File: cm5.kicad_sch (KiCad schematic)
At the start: 22 parts

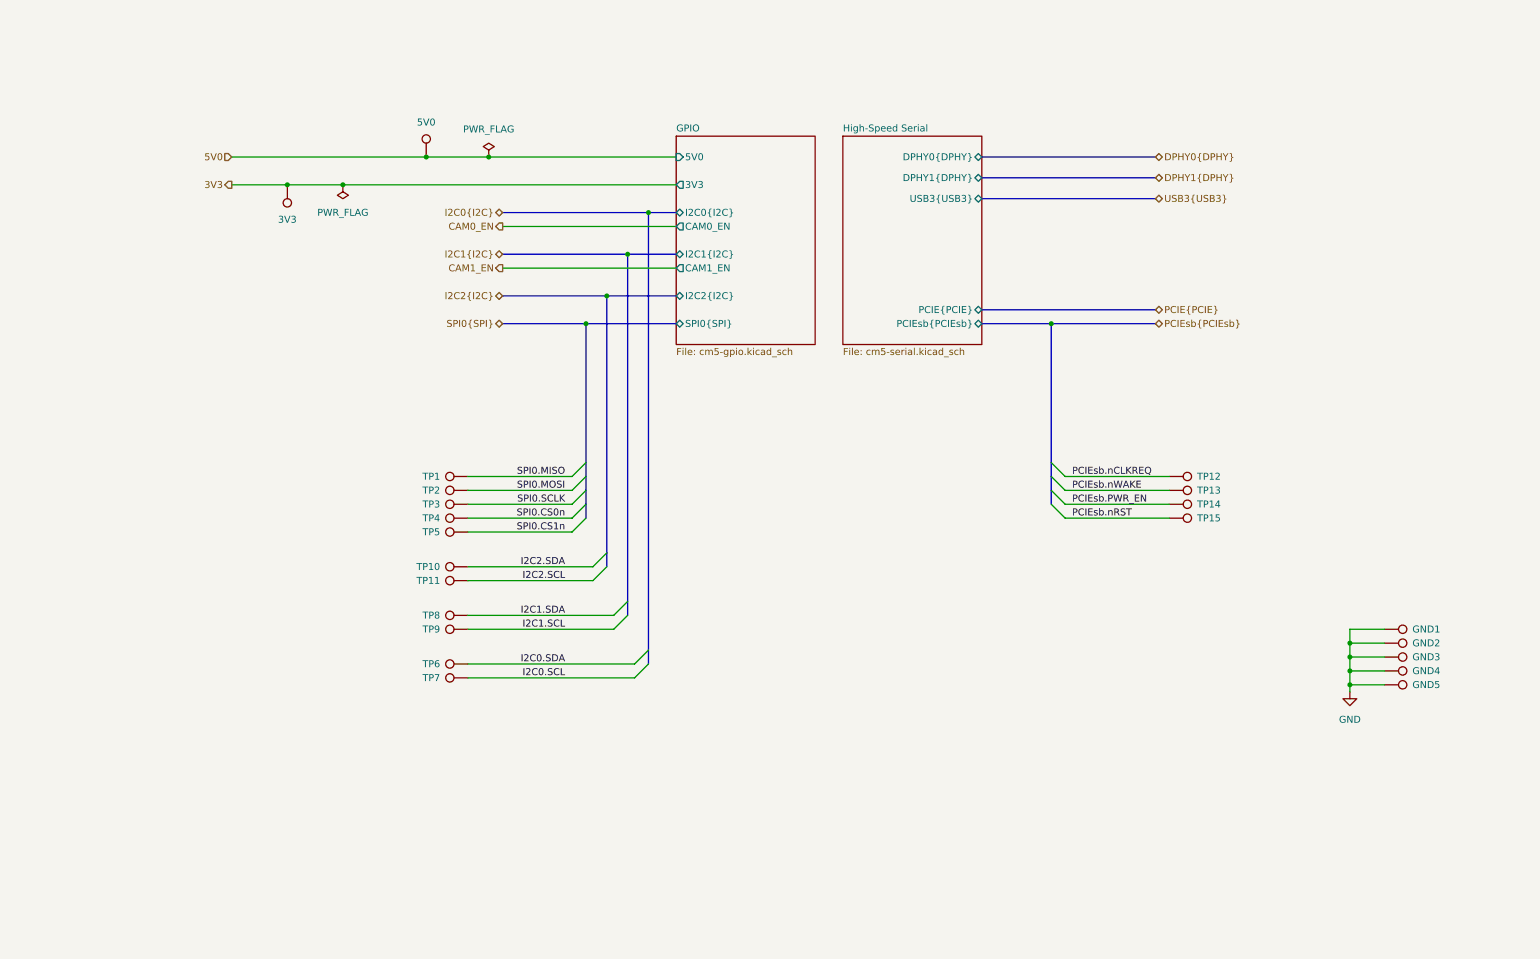
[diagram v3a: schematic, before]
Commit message: added conns to backplane
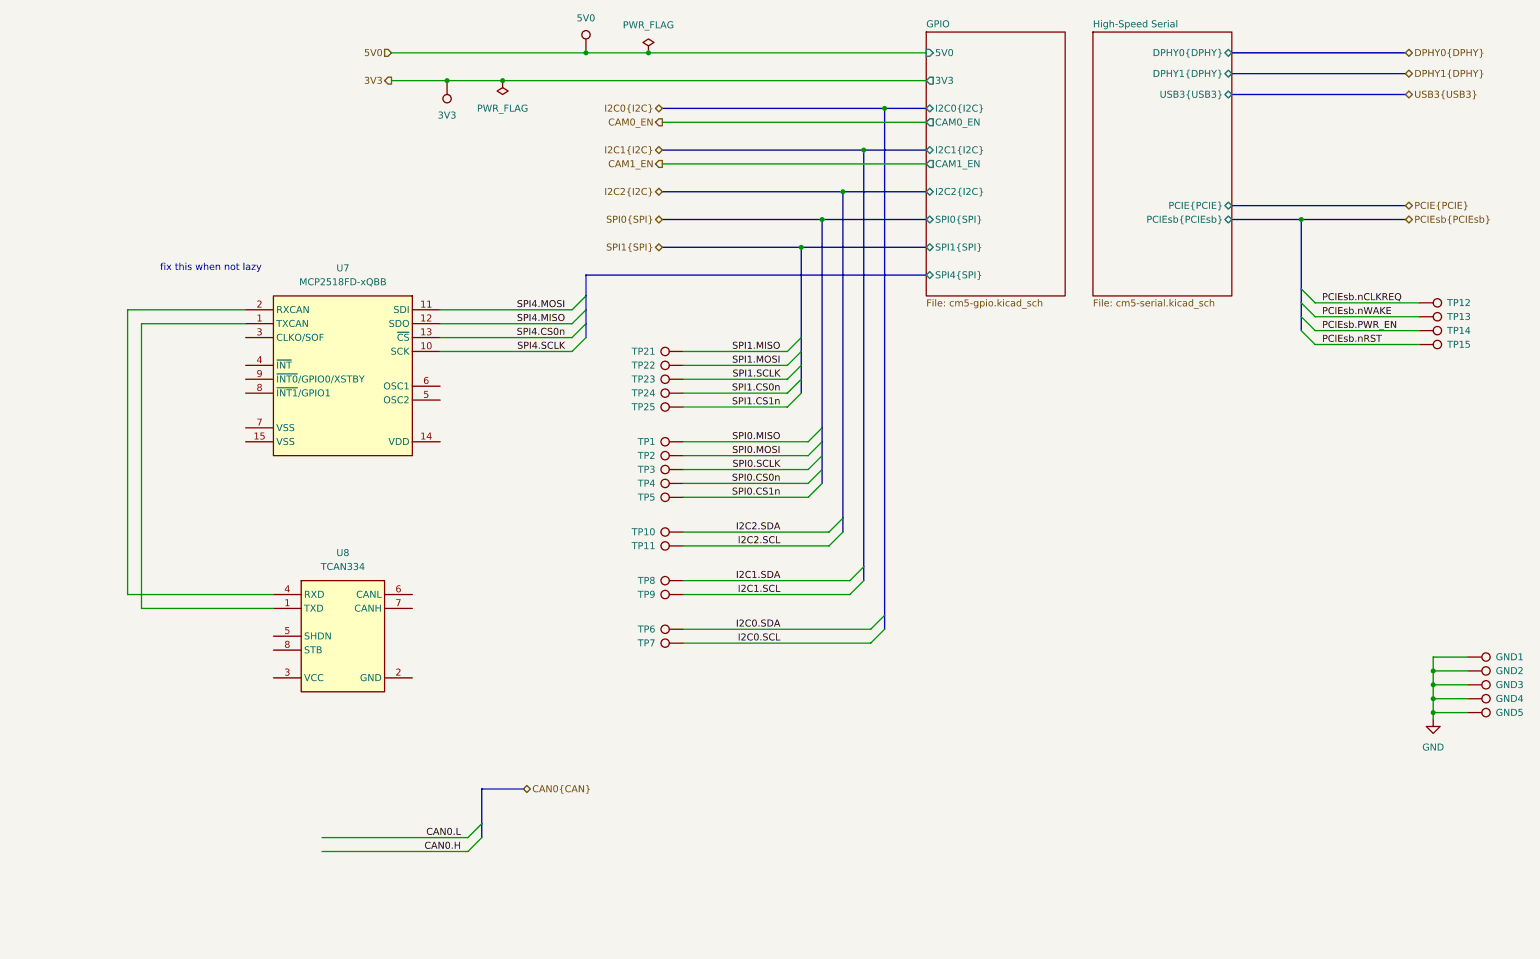
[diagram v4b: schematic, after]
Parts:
- added TP21, TP22, TP23, TP24, TP25: TestPoint, TestPoint:TestPoint_Pad_D1.0mm, symbol library:TestPoint
- added U7: MCP2518FD-xQBB, Package_DFN_QFN:DFN-14-1EP_3x4.5mm_P0.65mm_EP1.65x4.25mm, symbol Interface_CAN_LIN:MCP2518FD-xQBB
- added U8: TCAN334, Package_SO:JEITA_SOIC-8_3.9x4.9mm_P1.27mm, symbol Interface_CAN_LIN:TCAN334
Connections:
- new net: U7.1 (TXCAN), U8.1 (TXD)
- new net: U7.2 (RXCAN), U8.4 (RXD)
- new net SPI1.CS0n: TP24.1
- new net SPI1.CS1n: TP25.1
- new net SPI1.MISO: TP21.1
- new net SPI1.MOSI: TP22.1
- new net SPI1.SCLK: TP23.1
- new net SPI4.CS0n: U7.13 (~{CS})
- new net SPI4.MISO: U7.12 (SDO)
- new net SPI4.MOSI: U7.11 (SDI)
- new net SPI4.SCLK: U7.10 (SCK)
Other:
- sheet GPIO ports: added SPI1{SPI}, SPI4{SPI}; removed none
- note added: "fix this when not lazy"
- moved on the sheet: 3V3, 5V0, GND1, GND2, GND3, GND4, GND5, TP1, TP10, TP11, TP12, TP13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

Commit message: removed ublox
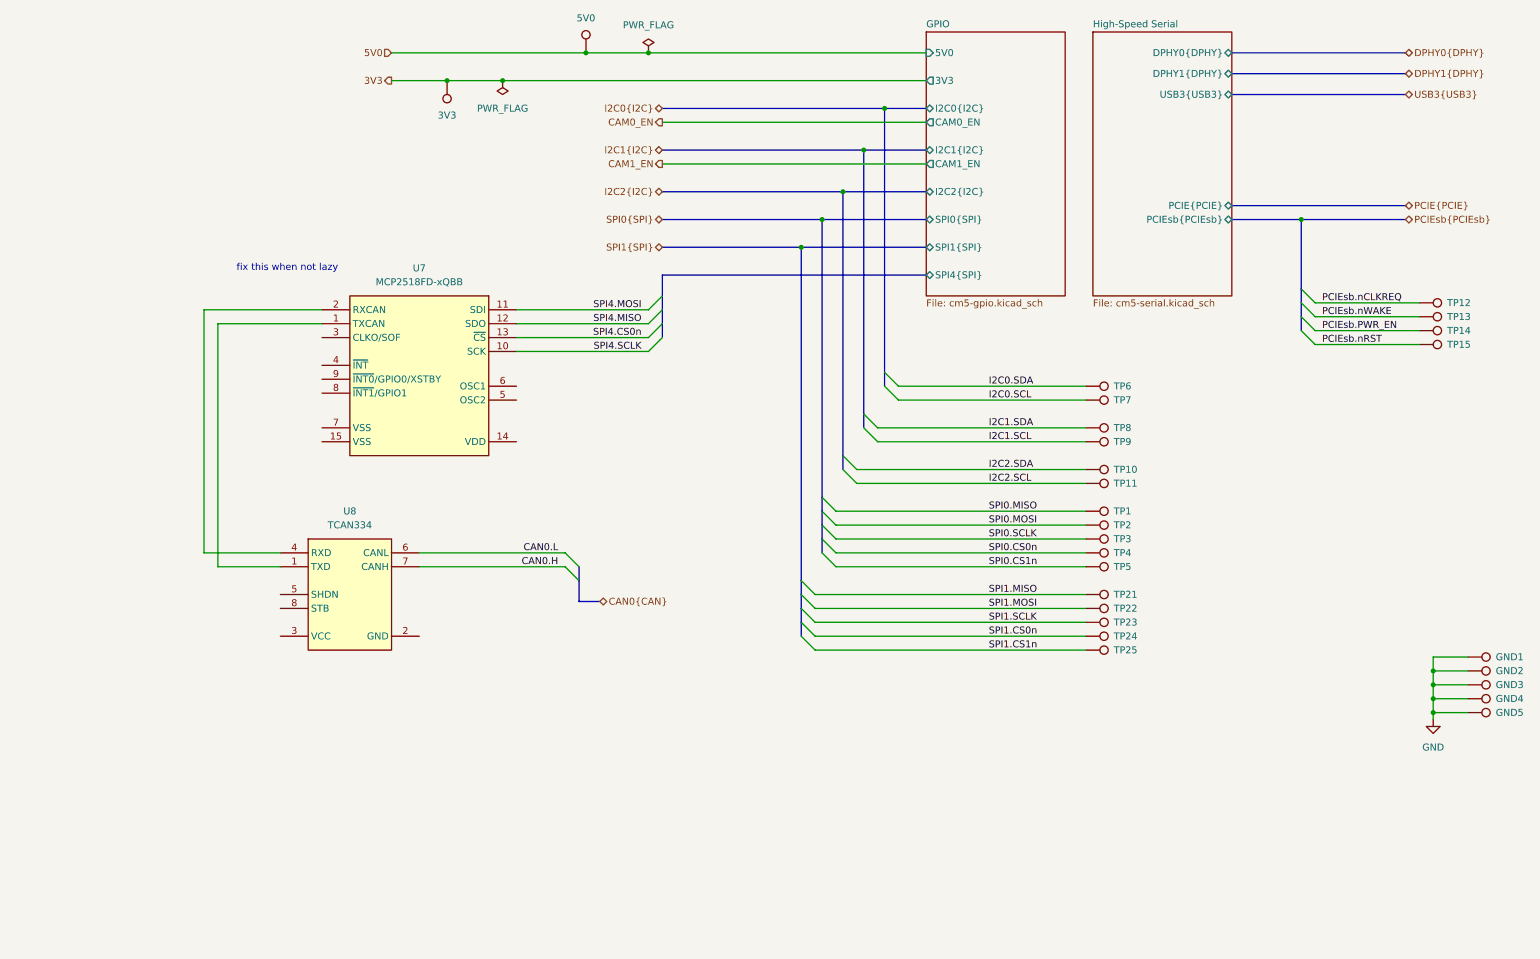
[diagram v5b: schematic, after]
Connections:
- net CAN0.H: now also U8.7 (CANH)
- net CAN0.L: now also U8.6 (CANL)
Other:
- moved on the sheet: TP1, TP10, TP11, TP2, TP21, TP22, TP23, TP24, TP25, TP3, TP4, TP5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

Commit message: defined can
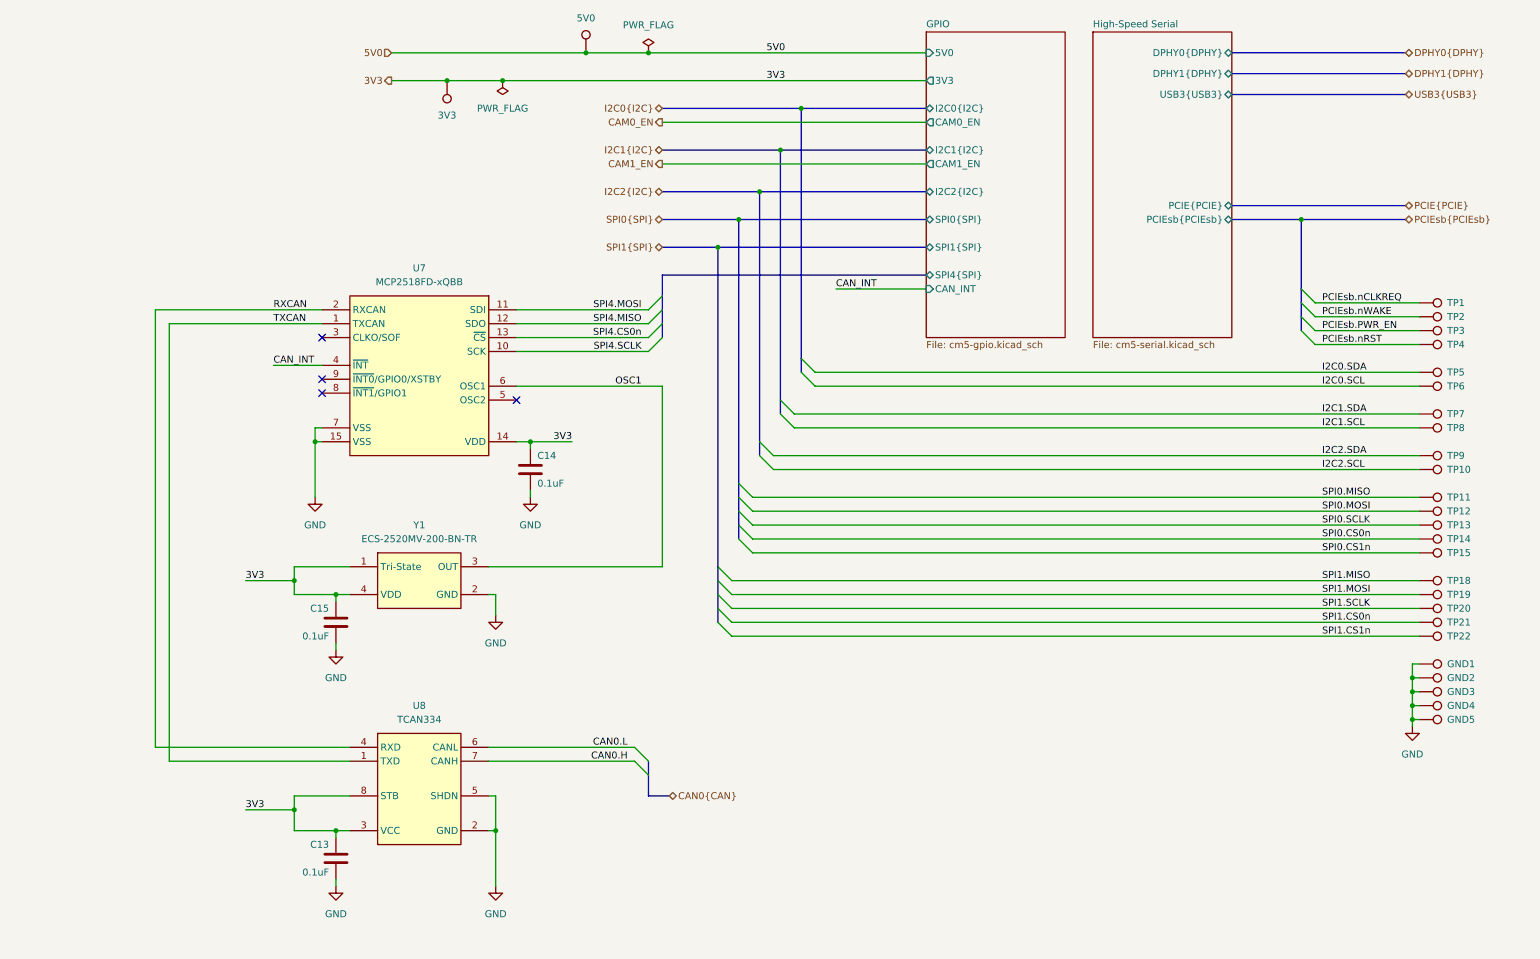
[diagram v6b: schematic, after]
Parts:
- added C13, C14, C15: 0.1uF, Capacitor_SMD:C_0402_1005Metric, symbol library:C
- added Y1: ECS-2520MV-200-BN-TR, Oscillator:Oscillator_SMD_ECS_2520MV-xxx-xx-4Pin_2.5x2.0mm, symbol Oscillator:ECS-2520MV-xxx-xx
- renumbered TP12 to TP1, TP11 to TP10, TP1 to TP11, TP2 to TP12, TP3 to TP13, TP4 to TP14, TP5 to TP15, TP21 to TP18, TP22 to TP19, TP13 to TP2, TP23 to TP20, TP24 to TP21, TP25 to TP22, TP14 to TP3, TP15 to TP4, TP6 to TP5, TP7 to TP6, TP8 to TP7, TP9 to TP8, TP10 to TP9
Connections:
- net 3V3: now also U7.14 (VDD), U8.3 (VCC), U8.8 (STB), C13.1, C14.1, C15.1, Y1.1 (Tri-State), Y1.4 (VDD)
- net GND: now also U7.15 (VSS), U7.7 (VSS), U8.2 (GND), U8.5 (SHDN), C13.2, C14.2, C15.2, Y1.2 (GND)
- net TXCAN: now reaches U7.1 (TXCAN), U8.1 (TXD)
- net RXCAN: now reaches U7.2 (RXCAN), U8.4 (RXD)
- net CAN_INT: now reaches U7.4 (~{INT})
- net OSC1: now reaches U7.6 (OSC1)
- net OSC1: now also Y1.3 (OUT)
- no-connect marks 0 -> 4
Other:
- sheet GPIO ports: added CAN_INT; removed none
- note removed: "fix this when not lazy"
- moved on the sheet: GND1, GND2, GND3, GND4, GND5, TP10, TP11, TP12, TP13, TP14, TP15, TP18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

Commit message: finished defining spi/i2c gpio, CAN, off-board signals
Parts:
- removed TP22: TestPoint, TestPoint:TestPoint_Pad_D1.0mm, symbol library:TestPoint
- added R13: 2.2K 1%, Resistor_SMD:R_0402_1005Metric, symbol library:R_US
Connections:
- net SPI0.CS0n is gone; now on net SPI1.CS0n: TP14.1
- net SPI0.CS1n is gone; now on net SPI1.CS1n: TP15.1
- net SPI0.MISO is gone; now on net SPI1.MISO: TP11.1
- net SPI0.MOSI is gone; now on net SPI1.MOSI: TP12.1
- net SPI0.SCLK is gone; now on net SPI1.SCLK: TP13.1
- net 3V3: now also R13.1
- net CAN_INT: now also R13.2
- net SPI1.CS0n: no longer TP21.1
- net SPI1.MISO: no longer TP18.1
- net SPI1.MOSI: no longer TP19.1
- net SPI1.SCLK: no longer TP20.1
- net SPI4.CS0n renamed SPI3.CS0n
- net SPI4.MISO renamed SPI3.MISO
- net SPI4.MOSI renamed SPI3.MOSI
- net SPI4.SCLK renamed SPI3.SCLK
- new net SPI2.CS0n: TP21.1
- new net SPI2.MISO: TP18.1
- new net SPI2.MOSI: TP19.1
- new net SPI2.SCLK: TP20.1
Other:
- sheet GPIO ports: added SPI2{SPI}, SPI3{SPI}; removed SPI0{SPI}, SPI4{SPI}
- moved on the sheet: GND1, GND2, GND3, GND4, GND5

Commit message: power planes and sensor placement
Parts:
- removed TP1, TP2, TP3, TP4: TestPoint, TestPoint:TestPoint_Pad_D1.0mm, symbol library:TestPoint
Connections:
- net CAN0.H renamed CAN0.P
- net CAN0.L renamed CAN0.N
